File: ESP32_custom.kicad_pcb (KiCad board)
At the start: 4 copper layers, 0 parts

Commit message: setting constraints
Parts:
- added C1: 100nF, Capacitor_SMD:C_0402_1005Metric, F.Cu at (144.7, 71.5)
- added C2: 100nF, Capacitor_SMD:C_0402_1005Metric, F.Cu at (144.7, 73.5)
- added C3: 100nF, Capacitor_SMD:C_0402_1005Metric, F.Cu at (144.7, 75.4)
- added C4: 100nF, Capacitor_SMD:C_0402_1005Metric, F.Cu at (144.7, 77.4)
- added C5: 100nF, Capacitor_SMD:C_0402_1005Metric, F.Cu at (144.7, 79.4)
- added C6: 100nF, Capacitor_SMD:C_0402_1005Metric, F.Cu at (144.7, 81.3)
- added J1: TYPE-C-31-M-12, TYPE-C-31-M-12:HRO_TYPE-C-31-M-12, F.Cu at (132.7, 109.0)
- added J2: Conn_01x16_Pin, Connector_PinHeader_2.00mm:PinHeader_1x16_P2.00mm_Vertical, F.Cu at (116.1, 72.5)
- added J3: Conn_01x16_Pin, Connector_PinHeader_2.00mm:PinHeader_1x16_P2.00mm_Vertical, F.Cu at (141.0, 62.7)
- added Q1: SS8050, Package_TO_SOT_SMD:SOT-23-3, F.Cu at (155.7, 102.3)
- added Q2: SS8050, Package_TO_SOT_SMD:SOT-23-3, F.Cu at (155.7, 106.8)
- added R1: 1K, Resistor_SMD:R_0402_1005Metric, F.Cu at (144.7, 91.2)
- added R10: 10K, Resistor_SMD:R_0402_1005Metric, F.Cu at (147.6, 99.1)
- added R2: 1K, Resistor_SMD:R_0402_1005Metric, F.Cu at (144.7, 93.2)
- added R3: 470, Resistor_SMD:R_0402_1005Metric, F.Cu at (144.7, 95.1)
- added R4: 470, Resistor_SMD:R_0402_1005Metric, F.Cu at (144.7, 97.1)
- added R5: 10K, Resistor_SMD:R_0402_1005Metric, F.Cu at (144.7, 99.1)
- added R6: 10K, Resistor_SMD:R_0402_1005Metric, F.Cu at (147.6, 91.2)
- added R7: 10K, Resistor_SMD:R_0402_1005Metric, F.Cu at (147.6, 93.2)
- added R8: 10K, Resistor_SMD:R_0402_1005Metric, F.Cu at (147.6, 95.1)
- added R9: 10K, Resistor_SMD:R_0402_1005Metric, F.Cu at (147.6, 97.1)
- added SW1: SW_Push, Button_Switch_SMD:SW_SPST_Omron_B3FS-100xP, F.Cu at (148.9, 86.2)
- added SW2: SW_Push, Button_Switch_SMD:SW_SPST_GT-TC155X, F.Cu at (153.7, 94.4)
- added U2: ESP32-WROOM-32E 8MB, KiCADv6:ESP32­WROOM­32E_EXP, F.Cu at (128.5, 67.3)
- added U3: CH340C, Package_SO:SOIC-16_3.9x9.9mm_P1.27mm, F.Cu at (150.3, 76.4)
- added U4: AMS1117-3.3, Package_TO_SOT_SMD:SOT-223-3_TabPin2, F.Cu at (148.2, 104.3)

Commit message: arranging footprint
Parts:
- J2, J3: footprint Connector_PinHeader_2.00mm:PinHeader_1x16_P2.00mm_Vertical -> Connector_PinHeader_2.54mm:PinHeader_1x16_P2.54mm_Vertical; moved to B.Cu
- SW2: footprint Button_Switch_SMD:SW_SPST_GT-TC155X -> Button_Switch_SMD:SW_SPST_Omron_B3FS-100xP
- moved Q1 41.1 mm to (119.1, 83.6), turned to 90 degrees
- moved Q2 39.1 mm to (124.2, 83.6), turned to 90 degrees
- moved SW2 35.4 mm to (119.9, 104.9), turned to 90 degrees
- moved C2 32.7 mm to (122.8, 97.8)
- moved U3 32.2 mm to (122.8, 93.2), turned to 90 degrees
- moved C6 31.8 mm to (118.3, 99.1)
- moved R7 28.0 mm to (121.7, 82.6), turned to -90 degrees
- moved R8 28.0 mm to (121.7, 84.6), turned to 90 degrees
- moved C1 25.6 mm to (125.5, 88.4)
- moved R2 24.8 mm to (120.4, 88.4)
- moved R10 24.7 mm to (129.8, 82.0), turned to 90 degrees
- moved R9 24.3 mm to (128.5, 82.0), turned to 90 degrees
- moved R4 23.9 mm to (120.8, 99.1)
- moved SW1 22.0 mm to (137.2, 104.8), turned to -90 degrees
- moved R1 22.0 mm to (122.9, 88.4)
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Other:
- board outline added: 33 x 50.3 mm

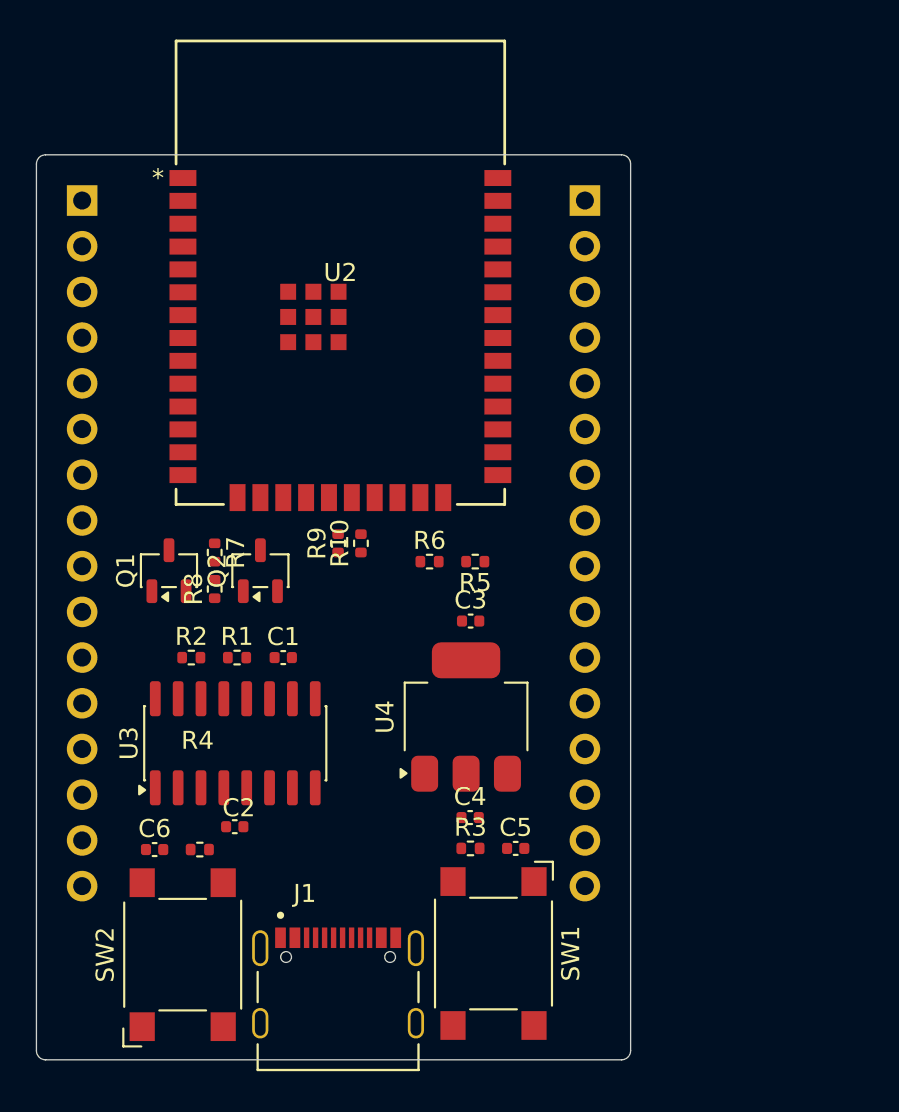
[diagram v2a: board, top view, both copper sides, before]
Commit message: change button footprint
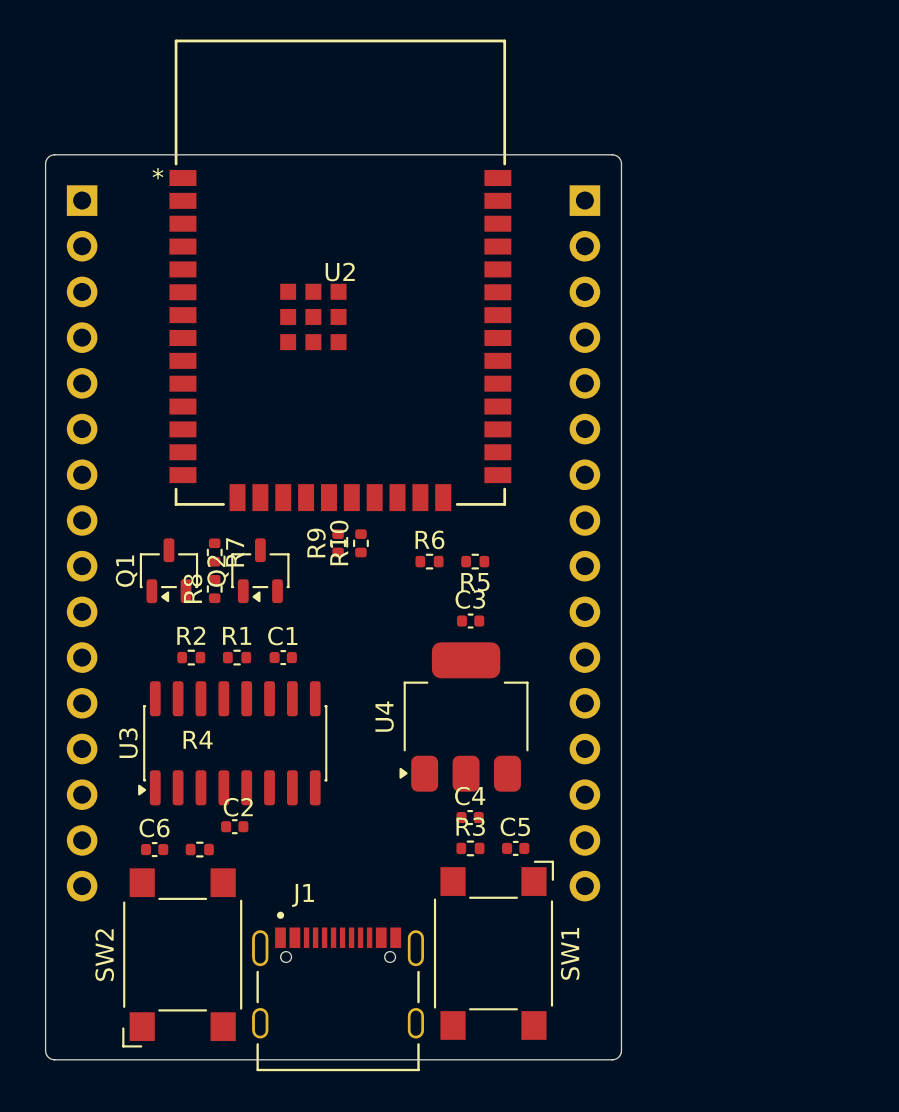
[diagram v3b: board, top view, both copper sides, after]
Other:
- board size 33 x 50.3 mm -> 32 x 50.3 mm
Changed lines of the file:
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@@
 	)
 	(gr_line
-		(start 111.76 60.96)
-		(end 111.76 110.236)
+		(start 112.268 60.96)
+		(end 112.268 110.236)
 		(stroke
 			(width 0.05)
@@
 	)
 	(gr_arc
-		(start 111.76 60.96)
-		(mid 111.90879 60.60079)
-		(end 112.268 60.452)
+		(start 112.268 60.96)
+		(mid 112.41679 60.60079)
+		(end 112.776 60.452)
 		(stroke
 			(width 0.05)
@@
 	)
 	(gr_line
-		(start 112.268 60.452)
-		(end 144.272 60.452)
+		(start 112.776 60.452)
+		(end 143.764 60.452)
 		(stroke
 			(width 0.05)
@@
 	)
 	(gr_arc
-		(start 112.268 110.744)
-		(mid 111.90879 110.59521)
-		(end 111.76 110.236)
+		(start 112.776 110.744)
+		(mid 112.41679 110.59521)
+		(end 112.268 110.236)
 		(stroke
 			(width 0.05)
@@
 	)
 	(gr_line
-		(start 112.268 110.744)
-		(end 144.272 110.744)
+		(start 112.776 110.744)
+		(end 143.764 110.744)
 		(stroke
 			(width 0.05)
@@
 	)
 	(gr_arc
-		(start 144.272 60.452)
-		(mid 144.63121 60.60079)
-		(end 144.78 60.96)
+		(start 143.764 60.452)
+		(mid 144.12321 60.60079)
+		(end 144.272 60.96)
 		(stroke
 			(width 0.05)
@@
 	)
 	(gr_line
-		(start 144.78 60.96)
-		(end 144.78 110.236)
+		(start 144.272 60.96)
+		(end 144.272 110.236)
 		(stroke
 			(width 0.05)
@@
 	)
 	(gr_arc
-		(start 144.78 110.236)
-		(mid 144.63121 110.59521)
-		(end 144.272 110.744)
+		(start 144.272 110.236)
+		(mid 144.12321 110.59521)
+		(end 143.764 110.744)
 		(stroke
 			(width 0.05)

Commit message: Put trace and Put net classes (uncomplete)
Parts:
- SW1, SW2: footprint Button_Switch_SMD:SW_SPST_Omron_B3FS-100xP -> Button_Switch_SMD:SW_SPST_B3U-1000P
- moved R2 18.8 mm to (137.9, 81.8), turned to 90 degrees
- moved R1 15.2 mm to (136.7, 81.8), turned to 90 degrees
- moved U4 13.6 mm to (122.3, 89.2), turned to 180 degrees
- moved U3 12.8 mm to (134.0, 86.9), turned to -90 degrees
- moved C2 11.8 mm to (127.8, 87.1), turned to -90 degrees
- moved C4 11.3 mm to (127.8, 89.4), turned to 90 degrees
- moved C3 9.72 mm to (127.8, 91.7), turned to -90 degrees
- moved C1 9.67 mm to (134.6, 91.4), turned to 180 degrees
- moved J1 7.88 mm to (128.3, 100.8)
- moved SW1 7.19 mm to (135.4, 97.9)
- moved SW2 7.14 mm to (121.1, 97.9), turned to -90 degrees
- moved C5 4.99 mm to (136.2, 94.5)
- moved R3 4.99 mm to (133.7, 94.5)
- moved C6 4.94 mm to (120.4, 94.6)
- moved R4 4.94 mm to (122.9, 94.6)
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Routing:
- net GND: track 0.00 -> 51.9 mm
- net /EN: track 0.00 -> 36.5 mm
- net +5V: track 0.00 -> 35.2 mm
- net /IO15: track 0.00 -> 33.7 mm, vias 0 -> 1
- net /IO2: track 0.00 -> 32.7 mm, vias 0 -> 1
- net /IO13: track 0.00 -> 28.0 mm, vias 0 -> 1
- net /IO0: track 0.00 -> 27.4 mm, vias 0 -> 1
- net /RX: track 0.00 -> 21.1 mm, vias 0 -> 1
- net /IO4: track 0.00 -> 20.6 mm, vias 0 -> 1
- net /IO17: track 0.00 -> 19.5 mm, vias 0 -> 1
- net /IO16: track 0.00 -> 19.4 mm, vias 0 -> 1
- net /TX: track 0.00 -> 19.4 mm, vias 0 -> 1
- net /IO12: track 0.00 -> 17.6 mm, vias 0 -> 1
- net /IO14: track 0.00 -> 16.8 mm, vias 0 -> 1
- net /IO5: track 0.00 -> 15.5 mm
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- added copper zone on In1.Cu, net GND
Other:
- board size 32 x 50.3 mm -> 32 x 42.2 mm

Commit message: define stackup (non-precise calculation
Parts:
- added R11: 5.1K, Resistor_SMD:R_0402_1005Metric, F.Cu at (131.3, 91.9)
- added R12: 5.1K, Resistor_SMD:R_0402_1005Metric, F.Cu at (131.3, 93.7)
- C3, C4, C5: value 100nF -> 10uF
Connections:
- net /D11 renamed /D-
- net /D22 renamed /D+
- C3 pad 1: +5V -> VCC
- C4 pad 2: VCC -> +5V
- J1 pad A4_B9: VCC -> +5V
- J1 pad A5: unconnected-(J1-CC1-PadA5) -> Net-(J1-CC1)
- J1 pad B4_A9: VCC -> +5V
- J1 pad B5: unconnected-(J1-CC2-PadB5) -> Net-(J1-CC2)
- J2 pad 1: +5V -> VCC
- Q2 pad 2: /IO0 -> /DTR
- Q2 pad 3: /DRT -> /IO0
- R5 pad 2: +5V -> VCC
- R7 pad 1: /DRT -> /DTR
- R9 pad 1: +5V -> VCC
- U2 pad 2: +5V -> VCC
- U4 pad 2: +5V -> VCC
- U4 pad 3: VCC -> +5V
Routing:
- net +5V: track 35.2 -> 3.13 mm
- net VCC: track 3.13 -> 19.3 mm
- net /DRT: track 2.70 -> 0.00 mm
- net (no net): track 0.00 -> 2.70 mm
- added copper zone on In2.Cu, net VCC

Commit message: routing DRC fail
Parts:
- moved U4 14.1 mm to (136.4, 88.5), turned to 90 degrees
- moved C4 11.4 mm to (138.2, 93.8), turned to 0 degrees
- moved R2 9.92 mm to (128.0, 82.3)
- moved C1 8.67 mm to (129.0, 84.8)
- moved Q2 8.51 mm to (118.3, 84.0), turned to 180 degrees
- moved C3 8.43 mm to (135.9, 93.8), turned to 180 degrees
- moved R7 8.36 mm to (117.3, 86.5), turned to 0 degrees
- moved C2 7.98 mm to (123.7, 94.0), turned to 0 degrees
- moved R1 7.38 mm to (129.3, 82.3)
- moved U3 7.35 mm to (127.0, 89.2), turned to 90 degrees
- moved Q1 7.08 mm to (118.3, 89.0), turned to 180 degrees
- moved R9 5.86 mm to (125.5, 82.3)
- moved R8 5.56 mm to (119.3, 86.5), turned to 180 degrees
- moved R12 5.13 mm to (126.2, 94.0), turned to 180 degrees
- moved R3 4.25 mm to (137.8, 95.8), turned to 180 degrees
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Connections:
- net Net-(J1-CC1) renamed /CC1
- net Net-(J1-CC2) renamed /CC2
- R1 pad 2: /RX -> /TX
- R2 pad 2: /TX -> /RX
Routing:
- net /EN: track 36.5 -> 66.4 mm, vias 0 -> 2
- net GND: track 51.9 -> 73.9 mm, vias 0 -> 15
- net /IO0: track 27.4 -> 47.5 mm, vias 1 -> 3
- net Net-(U3-RXD): track 2.41 -> 18.2 mm
- net Net-(U3-TXD): track 2.41 -> 16.9 mm
- net /DTR: track 0.00 -> 14.5 mm, vias 0 -> 2
- net /IO25: track 0.26 -> 13.0 mm, vias 0 -> 1
- net +5V: track 3.13 -> 15.5 mm, vias 0 -> 4
- net /TX: track 19.4 -> 29.4 mm, vias 1 -> 2
- net /RX: track 21.1 -> 30.2 mm, vias 1 -> 2
- net /RTS: track 1.75 -> 10.7 mm, vias 0 -> 3
- net Net-(U3-~{DTR}): track 2.31 -> 10.5 mm, vias 0 -> 2
- net VCC: track 19.3 -> 25.2 mm, vias 0 -> 3
- net Net-(U3-V3): track 0.00 -> 4.92 mm
- net /IO15: track 33.7 -> 29.0 mm
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- added copper zone on In2.Cu, net +5V

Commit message: fixed routed (DRC fails)
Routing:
- net GND: track 73.9 -> 65.1 mm, vias 15 -> 14
- net Net-(U3-RXD): track 18.2 -> 11.6 mm, vias 0 -> 2
- net Net-(U3-TXD): track 16.9 -> 11.0 mm, vias 0 -> 2
- net /RTS: track 10.7 -> 11.5 mm
- net /DTR: vias 2 -> 0
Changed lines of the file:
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@@
-	)
-	(via
-		(at 135.0518 74.3966)
-		(size 0.8)
-		(drill 0.4)
-		(layers "F.Cu" "B.Cu")
-		(net "GND")
 	)
 	(via
@@
 		(drill 0.4)
 		(layers "F.Cu" "B.Cu")
-		(net "GND")
-	)
-	(segment
-		(start 138.8872 78.232)
-		(end 135.0518 74.3966)
-		(width 0.6)
-		(layer "In1.Cu")
-		(net "GND")
-	)
-	(segment
-		(start 142.24 78.232)
-		(end 138.8872 78.232)
-		(width 0.6)
-		(layer "In1.Cu")
 		(net "GND")
 	)
@@
 	)
 	(segment
-		(start 122.174 89.662)
-		(end 121.412 88.9)
-		(width 0.25)
-		(layer "F.Cu")
-		(net "Net-(U3-RXD)")
-	)
-	(segment
-		(start 125.095 91.629)
-		(end 125.095 90.654001)
-		(width 0.25)
+		(start 129.286 83.099577)
+		(end 129.286 82.804)
+		(width 0.15)
 		(layer "F.Cu")
 		(net "Net-(U3-RXD)")
@@
 	)
 	(segment
-		(start 128.016 84.074)
-		(end 129.286 82.804)
-		(width 0.25)
-		(layer "F.Cu")
-		(net "Net-(U3-RXD)")
-	)
-	(segment
-		(start 124.102999 89.662)
-		(end 122.174 89.662)
-		(width 0.25)
-		(layer "F.Cu")
-		(net "Net-(U3-RXD)")
-	)
-	(segment
-		(start 121.412 84.836)
-		(end 122.174 84.074)
-		(width 0.25)
-		(layer "F.Cu")
-		(net "Net-(U3-RXD)")
-	)
-	(segment
-		(start 122.174 84.074)
-		(end 128.016 84.074)
-		(width 0.25)
-		(layer "F.Cu")
-		(net "Net-(U3-RXD)")
-	)
-	(segment
-		(start 125.095 90.654001)
-		(end 124.102999 89.662)
-		(width 0.25)
-		(layer "F.Cu")
-		(net "Net-(U3-RXD)")
-	)
-	(segment
-		(start 121.412 88.9)
-		(end 121.412 84.836)
-		(width 0.25)
-		(layer "F.Cu")
+		(start 125.758741 89.557993)
+		(end 125.758741 89.871454)
+		(width 0.15)
+		(layer "F.Cu")
+		(net "Net-(U3-RXD)")
+	)
+	(segment
+		(start 128.409577 83.976)
+		(end 129.286 83.099577)
+		(width 0.15)
+		(layer "F.Cu")
+		(net "Net-(U3-RXD)")
+	)
+	(segment
+		(start 125.758741 89.871454)
+		(end 125.095 90.535195)
+		(width 0.15)
+		(layer "F.Cu")
+		(net "Net-(U3-RXD)")
+	)
+	(segment
+		(start 125.095 90.535195)
+		(end 125.095 91.629)
+		(width 0.15)
+		(layer "F.Cu")
+		(net "Net-(U3-RXD)")
+	)
+	(via
+		(at 125.758741 89.557993)
+		(size 0.6)
+		(drill 0.3)
+		(layers "F.Cu" "B.Cu")
+		(net "Net-(U3-RXD)")
+	)
+	(via
+		(at 128.409577 83.976)
+		(size 0.6)
+		(drill 0.3)
+		(layers "F.Cu" "B.Cu")
+		(net "Net-(U3-RXD)")
+	)
+	(segment
+		(start 125.758741 89.474462)
+		(end 125.857 89.376203)
+		(width 0.15)
+		(layer "B.Cu")
+		(net "Net-(U3-RXD)")
+	)
+	(segment
+		(start 125.857 89.376203)
+		(end 125.857 88.830685)
+		(width 0.15)
+		(layer "B.Cu")
+		(net "Net-(U3-RXD)")
+	)
+	(segment
+		(start 126.717 83.976)
+		(end 128.409577 83.976)
+		(width 0.15)
+		(layer "B.Cu")
+		(net "Net-(U3-RXD)")
+	)
+	(segment
+		(start 125.984 88.703685)
+		(end 125.984 84.709)
+		(width 0.15)
+		(layer "B.Cu")
+		(net "Net-(U3-RXD)")
+	)
+	(segment
+		(start 125.758741 89.557993)
+		(end 125.758741 89.474462)
+		(width 0.15)
+		(layer "B.Cu")
+		(net "Net-(U3-RXD)")
+	)
+	(segment
+		(start 125.857 88.830685)
+		(end 125.984 88.703685)
+		(width 0.15)
+		(layer "B.Cu")
+		(net "Net-(U3-RXD)")
+	)
+	(segment
+		(start 125.984 84.709)
+		(end 126.717 83.976)
+		(width 0.15)
+		(layer "B.Cu")
 		(net "Net-(U3-RXD)")
 	)
@@
 	)
 	(segment
+		(start 123.9158 82.423)
+		(end 132.207 82.423)
+		(width 0.25)
+		(layer "B.Cu")
+		(net "/IO0")
+	)
+	(segment
+		(start 132.207 82.423)
+		(end 134.366 80.264)
+		(width 0.25)
+		(layer "B.Cu")
+		(net "/IO0")
+	)
+	(segment
 		(start 134.366 78.740344)
 		(end 134.875241 78.231103)
@@
 	(segment
 		(start 123.5348 82.804)
-		(end 131.826 82.804)
+		(end 123.9158 82.423)
 		(width 0.25)
 		(layer "B.Cu")
@@
 	)
 	(segment
-		(start 131.826 82.804)
-		(end 134.366 80.264)
-		(width 0.25)
-		(layer "B.Cu")
-		(net "/IO0")
-	)
-	(segment
 		(start 142.24 96.012)
 		(end 138.176 91.948)
@@
 	)
 	(segment
-		(start 123.825 91.629)
-		(end 123.825 90.654001)
-		(width 0.25)
+		(start 126.873 83.185)
+		(end 127.635 83.185)
+		(width 0.15)
 		(layer "F.Cu")
 		(net "Net-(U3-TXD)")
 	)
 	(segment
-		(start 123.340999 90.17)
-		(end 121.92 90.17)
-		(width 0.25)
+		(start 125.095 89.535)
+		(end 123.825 90.805)
+		(width 0.15)
 		(layer "F.Cu")
 		(net "Net-(U3-TXD)")
 	)
 	(segment
-		(start 120.904 89.154)
-		(end 120.904 84.582)
-		(width 0.25)
+		(start 127.635 83.185)
+		(end 128.016 82.804)
+		(width 0.15)
 		(layer "F.Cu")
 		(net "Net-(U3-TXD)")
 	)
 	(segment
-		(start 121.92 90.17)
-		(end 120.904 89.154)
-		(width 0.25)
+		(start 123.825 90.805)
+		(end 123.825 91.629)
+		(width 0.15)
 		(layer "F.Cu")
 		(net "Net-(U3-TXD)")
 	)
 	(segment
-		(start 120.904 84.582)
-		(end 121.9962 83.4898)
-		(width 0.25)
+		(start 125.095 89.027)
+		(end 125.095 89.535)
+		(width 0.15)
 		(layer "F.Cu")
 		(net "Net-(U3-TXD)")
 	)
-	(segment
-		(start 127.3302 83.4898)
-		(end 128.016 82.804)
-		(width 0.25)
-		(layer "F.Cu")
+	(via
+		(at 125.095 89.027)
+		(size 0.6)
+		(drill 0.3)
+		(layers "F.Cu" "B.Cu")
 		(net "Net-(U3-TXD)")
 	)
-	(segment
-		(start 123.825 90.654001)
-		(end 123.340999 90.17)
-		(width 0.25)
-		(layer "F.Cu")
+	(via
+		(at 126.873 83.185)
+		(size 0.6)
+		(drill 0.3)
+		(layers "F.Cu" "B.Cu")
 		(net "Net-(U3-TXD)")
 	)
 	(segment
-		(start 121.9962 83.4898)
-		(end 127.3302 83.4898)
-		(width 0.25)
-		(layer "F.Cu")
+		(start 125.095 89.027)
+		(end 125.4644 88.6576)
+		(width 0.15)
+		(layer "B.Cu")
+		(net "Net-(U3-TXD)")
+	)
+	(segment
+		(start 125.4644 88.6576)
+		(end 125.4644 84.5936)
+		(width 0.15)
+		(layer "B.Cu")
+		(net "Net-(U3-TXD)")
+	)
+	(segment
+		(start 125.4644 84.5936)
+		(end 126.873 83.185)
+		(width 0.15)
+		(layer "B.Cu")
 		(net "Net-(U3-TXD)")
 	)
@@
 	)
 	(segment
-		(start 119.4485 88.091001)
+		(start 120.904 89.154)
+		(end 120.142 89.154)
+		(width 0.25)
+		(layer "F.Cu")
+		(net "/RTS")
+	)
+	(segment
+		(start 119.4485 88.4605)
+		(end 119.4485 88.091001)
+		(width 0.25)
+		(layer "F.Cu")
+		(net "/RTS")
+	)
+	(segment
+		(start 120.142 89.154)
 		(end 119.4485 88.4605)
-		(width 0.25)
-		(layer "F.Cu")
-		(net "/RTS")
-	)
-	(segment
-		(start 119.4485 88.4605)
-		(end 120.142 89.154)
 		(width 0.25)
 		(layer "F.Cu")
@@
 	)
 	(via
-		(at 120.142 89.154)
+		(at 120.904 89.154)
 		(size 0.6)
 		(drill 0.3)
@@
 	)
 	(segment
-		(start 116.789 86.501001)
-		(end 116.789 85.754619)
+		(start 126.8476 84.836)
+		(end 125.8316 83.82)
 		(width 0.25)
 		(layer "F.Cu")
@@
 	)
 	(segment
-		(start 116.789 85.754619)
-		(end 119.4485 83.095119)
+		(start 121.9708 83.82)
+		(end 121.2596 83.1088)
+		(width 0.25)
+		(layer "F.Cu")
+		(net "/DTR")
+	)
+	(segment
+		(start 119.4485 83.1165)
+		(end 119.4485 83.011001)
 		(width 0.25)
 		(layer "F.Cu")
@@
 	)
 	(segment
-		(start 119.4485 83.095119)
-		(end 119.4485 83.011001)
+		(start 116.789 85.776)
+		(end 119.4485 83.1165)
+		(width 0.25)
+		(layer "F.Cu")
+		(net "/DTR")
+	)
+	(segment
+		(start 128.552 84.836)
+		(end 126.8476 84.836)
+		(width 0.25)
+		(layer "F.Cu")
+		(net "/DTR")
+	)
+	(segment
+		(start 125.8316 83.82)
+		(end 121.9708 83.82)
+		(width 0.25)
+		(layer "F.Cu")
+		(net "/DTR")
+	)
+	(segment
+		(start 116.789 86.501001)
+		(end 116.789 85.776)
 		(width 0.25)
 		(layer "F.Cu")
@@
 		(net "/DTR")
 	)
-	(segment
-		(start 128.552 84.836)
-		(end 126.8476 84.836)
-		(width 0.25)
-		(layer "F.Cu")
-		(net "/DTR")
-	)
-	(via
-		(at 126.8476 84.836)
-		(size 0.6)
-		(drill 0.3)
-		(layers "F.Cu" "B.Cu")
-		(net "/DTR")
-	)
-	(via
-		(at 121.2596 83.1088)
-		(size 0.6)
-		(drill 0.3)
-		(layers "F.Cu" "B.Cu")
-		(net "/DTR")
-	)
-	(segment
-		(start 121.92 83.7692)
-		(end 121.2596 83.1088)
-		(width 0.25)
-		(layer "In1.Cu")
-		(net "/DTR")
-	)
-	(segment
-		(start 125.7808 83.7692)
-		(end 121.92 83.7692)
-		(width 0.25)
-		(layer "In1.Cu")
-		(net "/DTR")
-	)
-	(segment
-		(start 126.8476 84.836)
-		(end 125.7808 83.7692)
-		(width 0.25)
-		(layer "In1.Cu")
-		(net "/DTR")
-	)
